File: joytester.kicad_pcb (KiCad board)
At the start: 2 copper layers, 80 x 100 mm, 51 parts, among them J1 DB9_Male, J2 USB_B, J3 USB_C_Receptacle_PowerOnly_6P, J4 USB_B_Mini, J5 USB_B_Micro, SW1 C64MODESW, SW2 POWER, SW3 POWER, U1 4070, U2 74HC86

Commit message: minor update
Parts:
- added REF**: KiCad-Logo2_8mm_SilkScreen, Symbol:KiCad-Logo2_8mm_SilkScreen, B.Cu at (229.7, 50.8)
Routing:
- net /F2F3MODE: track 186.0 -> 184.1 mm
- net /F2LED: track 42.4 -> 40.6 mm
- net /RBTN: track 87.6 -> 86.0 mm
- net /LBTN: track 81.2 -> 79.9 mm
- net Net-(D5-A): track 31.9 -> 30.9 mm
- net /F3BTN: track 94.6 -> 93.7 mm
- net /F3LED: track 55.1 -> 54.3 mm
- net Net-(D7-A): track 40.0 -> 39.2 mm
- net Net-(D3-A): track 60.8 -> 60.1 mm
- net /F2BTN: track 83.5 -> 82.8 mm
- net GND: vias 240 -> 243

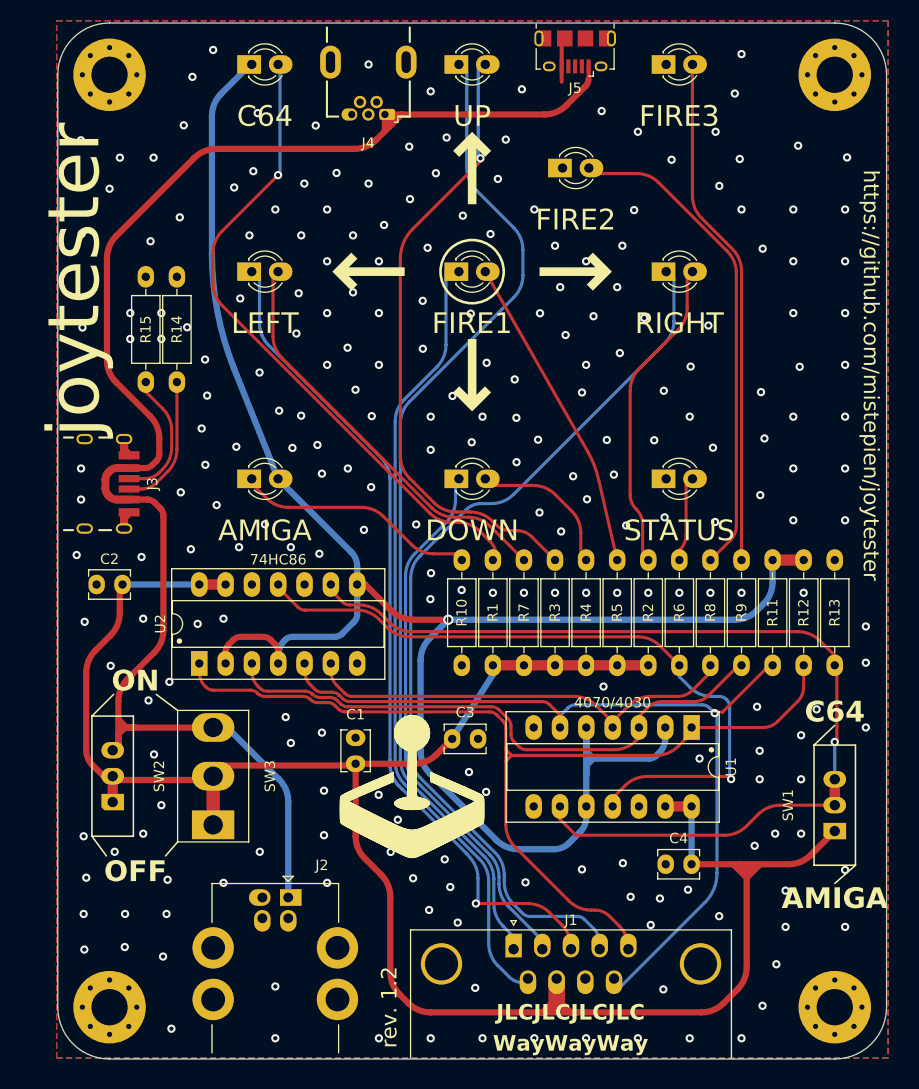
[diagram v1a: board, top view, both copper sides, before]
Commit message: update of Micro USB footprint
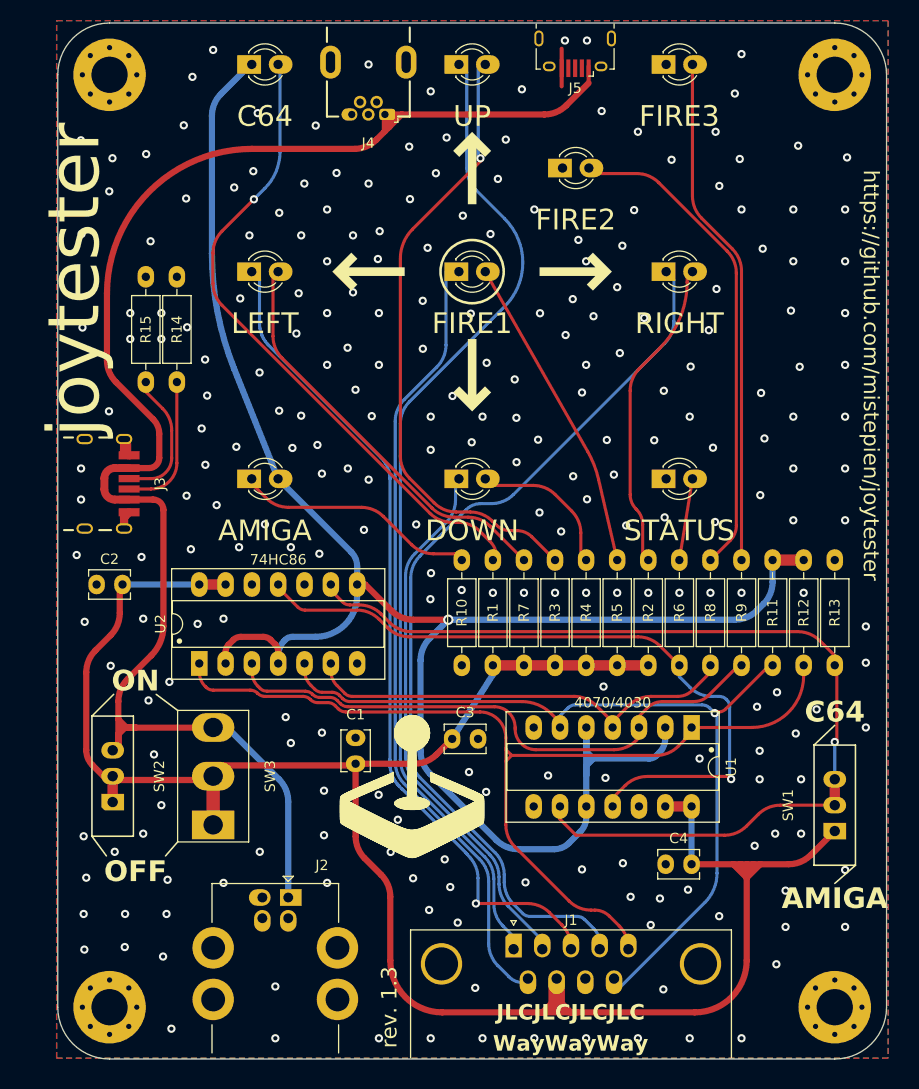
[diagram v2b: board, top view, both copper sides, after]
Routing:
- net GND: track 7.43 -> 8.95 mm, vias 243 -> 249
- net /F2BTN: track 82.8 -> 81.7 mm
- net /F2F3MODE: track 184.1 -> 183.4 mm
- net VCC: track 204.0 -> 203.3 mm
- net /F3BTN: track 93.7 -> 92.9 mm
- net Net-(J3-CC2): track 13.2 -> 13.8 mm
- added copper zone on F.Cu, net /F3BTN
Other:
- board text removed: "----------------- | U1 | U2 | ================= | 4070 | x | ----------------- | x | 74HC86 | -----------------"
